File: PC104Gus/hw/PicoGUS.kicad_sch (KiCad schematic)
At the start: 37 parts, among them J1 Conn_02x32_Odd_Even, J11 AudioJack3, J12 AudioJack3, J3 Conn_01x02_Pin, J4 IRQDMA_JP, J5 Conn_01x04_Pin, J6 UART_TX, U1 SN74CB3T3257, U10 74LVC1G00, U2 SN74CB3T3257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

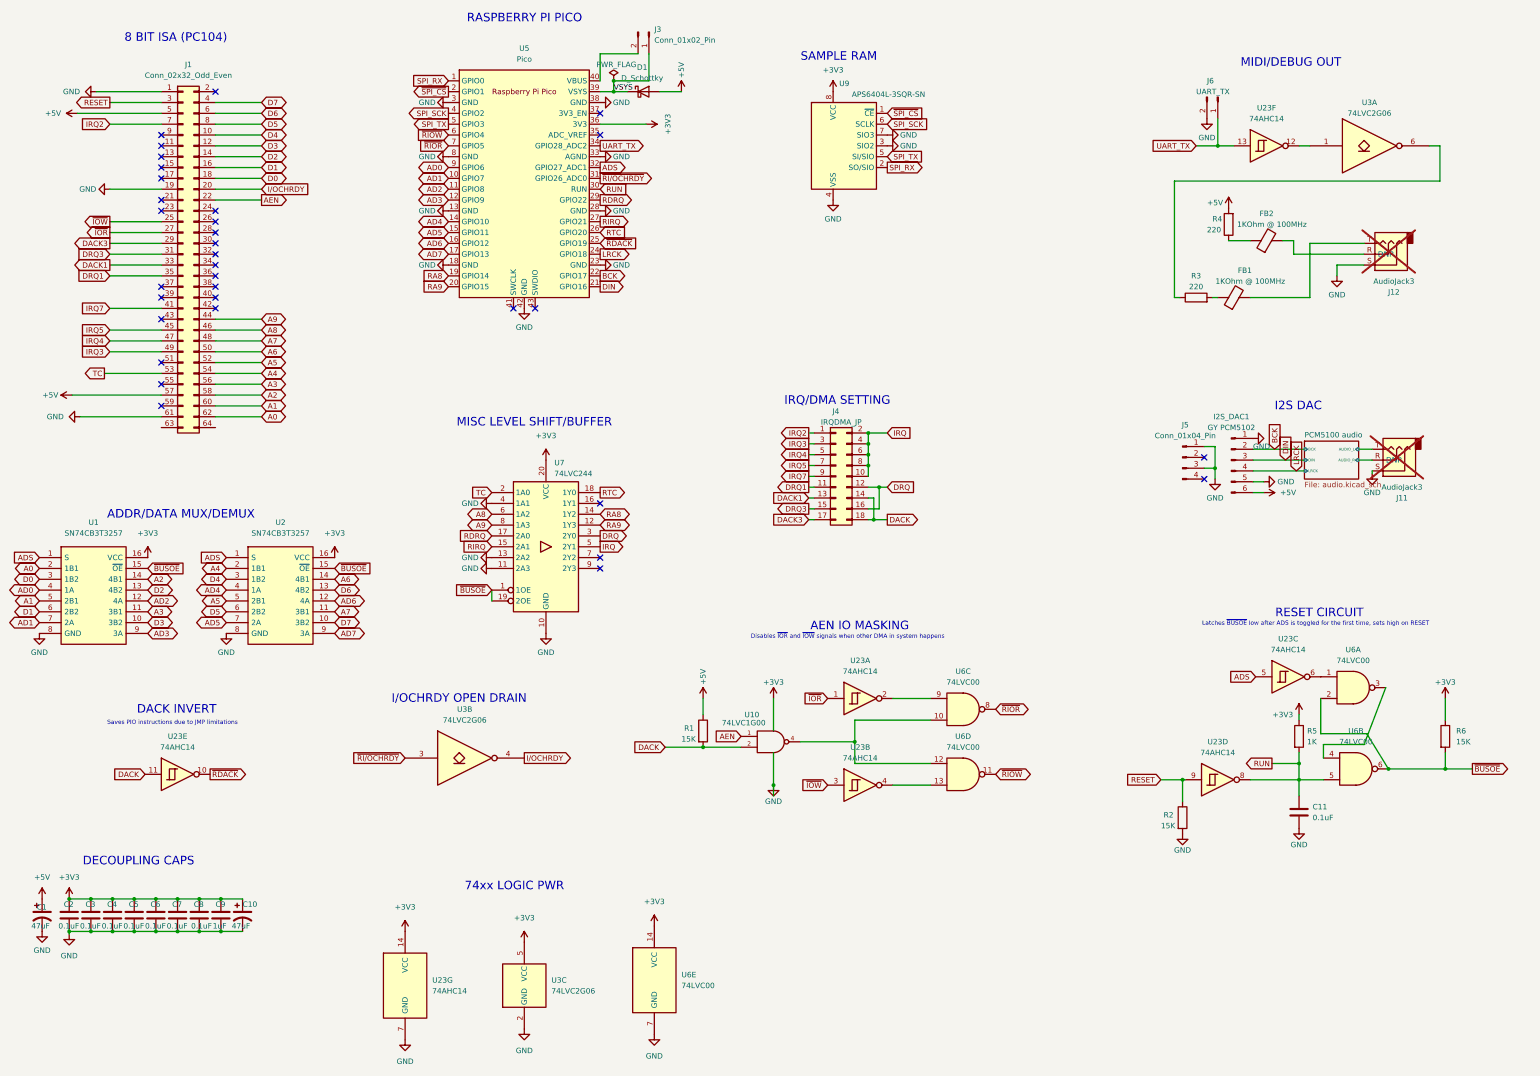
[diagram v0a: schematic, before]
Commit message: PC104GUS production files
Production files generated. This build worked!
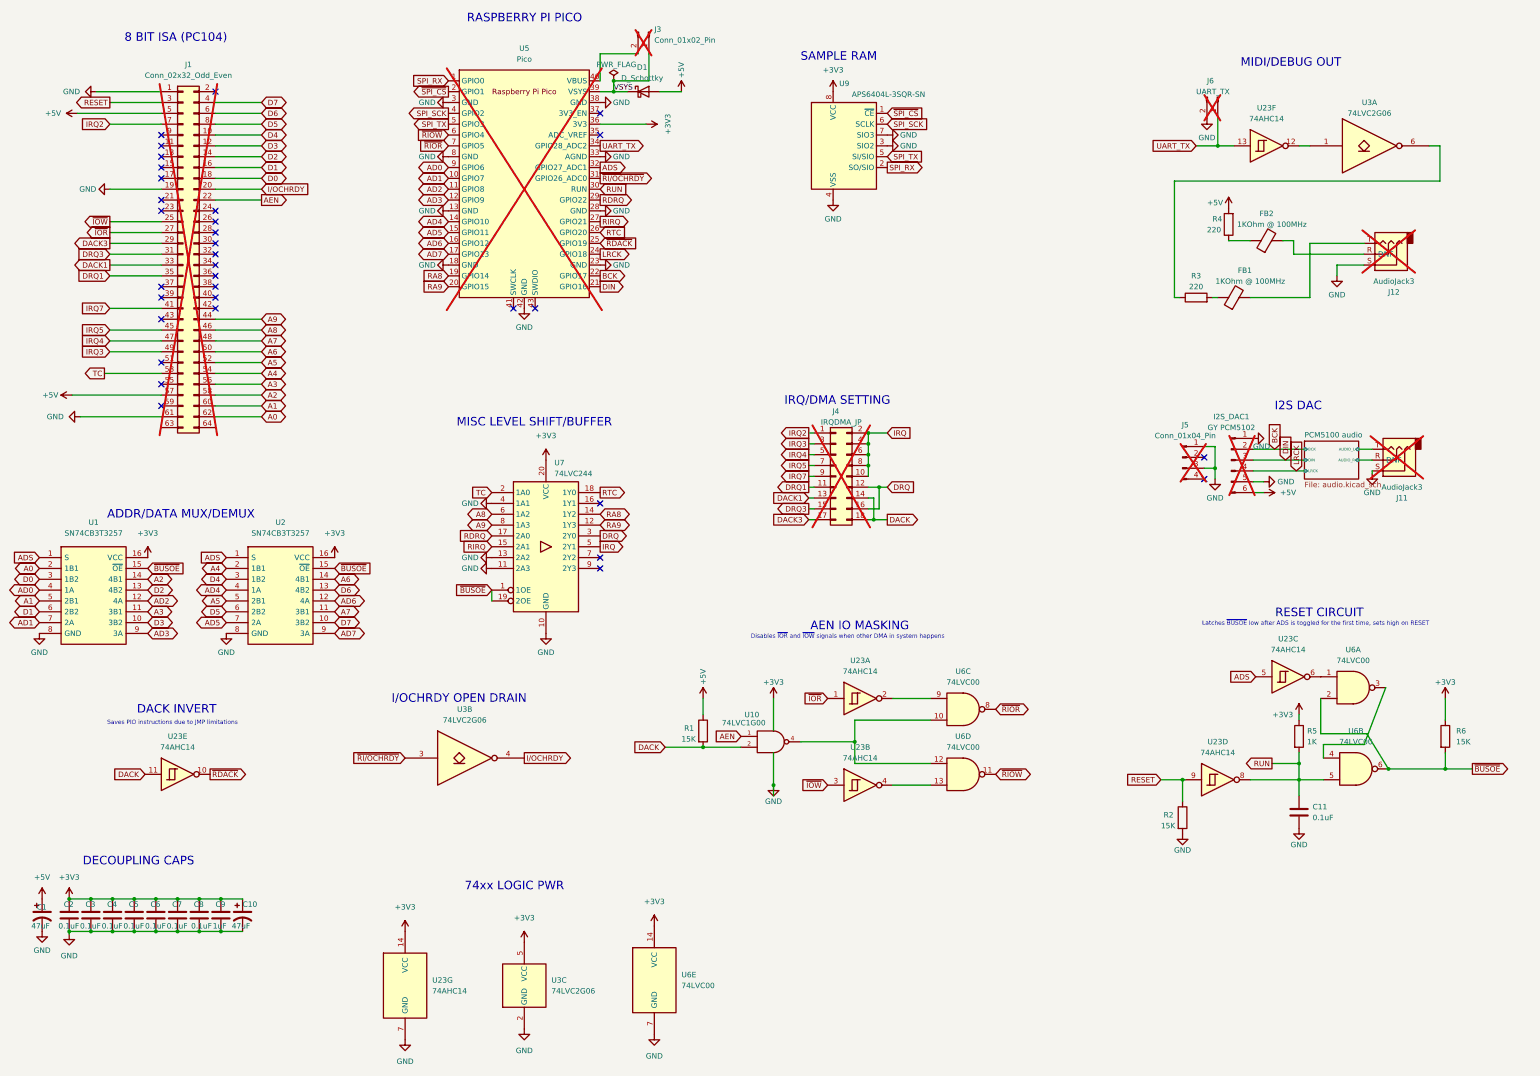
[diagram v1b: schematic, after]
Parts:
- I2S_DAC1, J1, J3, J5, J6: LCSC (none) -> DNF; now not fitted
- J11, J12: LCSC DNP -> DNF
- J4: LCSC C492426 -> DNF; now not fitted
- U23: LCSC (none) -> C5510
- U3: LCSC (none) -> C402162
- U5: LCSC C2905423 -> DNF; now not fitted
- U6: LCSC (none) -> C526338
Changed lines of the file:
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@@
 			)
 		)
+		(property "LCSC" "C402162"
+			(at 163.83 262.89 0)
+			(effects
+				(font
+					(size 1.27 1.27)
+				)
+				(hide yes)
+			)
+		)
 		(pin "3"
 		)
@@
 			)
 		)
+		(property "LCSC" "C5510"
+			(at 337.82 66.04 0)
+			(effects
+				(font
+					(size 1.27 1.27)
+				)
+				(hide yes)
+			)
+		)
 		(pin "6"
 		)
@@
 			)
 		)
+		(property "LCSC" "C5510"
+			(at 326.39 214.63 0)
+			(effects
+				(font
+					(size 1.27 1.27)
+				)
+				(hide yes)
+			)
+		)
 		(pin "6"
 		)
@@
 		(in_bom yes)
 		(on_board yes)
-		(dnp no)
+		(dnp yes)
 		(property "Reference" "I2S_DAC1"
 			(at 329.565 129.54 0)
@@
 			)
 		)
+		(property "LCSC" "DNF"
+			(at 329.565 139.7 0)
+			(effects
+				(font
+					(size 1.27 1.27)
+				)
+				(hide yes)
+			)
+		)
 		(pin "1"
 		)
@@
 			)
 		)
+		(property "LCSC" "C526338"
+			(at 194.31 261.62 0)
+			(effects
+				(font
+					(size 1.27 1.27)
+				)
+				(hide yes)
+			)
+		)
 		(pin "13"
 		)
@@
 		(in_bom yes)
 		(on_board yes)
-		(dnp no)
+		(dnp yes)
 		(fields_autoplaced yes)
 		(property "Reference" "J3"
@@
 			)
 		)
+		(property "LCSC" "DNF"
+			(at 193.04 39.37 90)
+			(effects
+				(font
+					(size 1.27 1.27)
+				)
+				(hide yes)
+			)
+		)
 		(pin "1"
 		)
@@
 			)
 		)
+		(property "LCSC" "C402162"
+			(at 363.22 66.04 0)
+			(effects
+				(font
+					(size 1.27 1.27)
+				)
+				(hide yes)
+			)
+		)
 		(pin "3"
 		)
@@
 		(in_bom yes)
 		(on_board yes)
-		(dnp no)
+		(dnp yes)
 		(fields_autoplaced yes)
 		(property "Reference" "U5"
@@
 			)
 		)
-		(property "LCSC" "C2905423"
+		(property "LCSC" "DNF"
 			(at 163.83 43.18 0)
 			(effects
@@
 			)
 		)
+		(property "LCSC" "C526338"
+			(at 358.775 212.09 0)
+			(effects
+				(font
+					(size 1.27 1.27)
+				)
+				(hide yes)
+			)
+		)
 		(pin "13"
 		)
@@
 			)
 		)
+		(property "LCSC" "C526338"
+			(at 266.7 198.12 0)
+			(effects
+				(font
+					(size 1.27 1.27)
+				)
+				(hide yes)
+			)
+		)
 		(pin "13"
 		)
@@
 			)
 		)
+		(property "LCSC" "C402162"
+			(at 151.13 209.55 0)
+			(effects
+				(font
+					(size 1.27 1.27)
+				)
+				(hide yes)
+			)
+		)
 		(pin "3"
 		)
@@
 			)
 		)
+		(property "LCSC" "C5510"
+			(at 242.57 215.9 0)
+			(effects
+				(font
+					(size 1.27 1.27)
+				)
+				(hide yes)
+			)
+		)
 		(pin "6"
 		)
@@
 			)
 		)
+		(property "LCSC" "C526338"
+			(at 358.14 193.04 0)
+			(effects
+				(font
+					(size 1.27 1.27)
+				)
+				(hide yes)
+			)
+		)
 		(pin "13"
 		)
@@
 		(in_bom yes)
 		(on_board yes)
-		(dnp no)
+		(dnp yes)
 		(property "Reference" "J4"
 			(at 236.855 128.27 0)
@@
 			)
 		)
-		(property "LCSC" "C492426"
+		(property "LCSC" "DNF"
 			(at 236.855 128.27 0)
 			(effects
@@
 			)
 		)
+		(property "LCSC" "C5510"
+			(at 82.55 213.36 0)
+			(effects
+				(font
+					(size 1.27 1.27)
+				)
+				(hide yes)
+			)
+		)
 		(pin "6"
 		)
@@
 		(in_bom yes)
 		(on_board yes)
-		(dnp no)
+		(dnp yes)
 		(fields_autoplaced yes)
 		(property "Reference" "J5"
@@
 			)
 		)
+		(property "LCSC" "DNF"
+			(at 318.135 139.065 0)
+			(effects
+				(font
+					(size 1.27 1.27)
+				)
+				(hide yes)
+			)
+		)
 		(pin "1"
 		)
@@
 			)
 		)
+		(property "LCSC" "C5510"
+			(at 242.57 195.58 0)
+			(effects
+				(font
+					(size 1.27 1.27)
+				)
+				(hide yes)
+			)
+		)
 		(pin "6"
 		)
@@
 		(in_bom yes)
 		(on_board yes)
-		(dnp no)
+		(dnp yes)
 		(property "Reference" "J6"
 			(at 323.85 50.8 90)
@@
 			)
 		)
+		(property "LCSC" "DNF"
+			(at 326.39 54.61 90)
+			(effects
+				(font
+					(size 1.27 1.27)
+				)
+				(hide yes)
+			)
+		)
 		(pin "1"
 		)
@@
 			)
 		)
-		(property "LCSC" "DNP"
+		(property "LCSC" "DNF"
 			(at 367.665 139.7 0)
 			(effects
@@
 			)
 		)
+		(property "LCSC" "C526338"
+			(at 266.7 213.36 0)
+			(effects
+				(font
+					(size 1.27 1.27)
+				)
+				(hide yes)
+			)
+		)
 		(pin "13"
 		)
@@
 			)
 		)
-		(property "LCSC" "DNP"
+		(property "LCSC" "DNF"
 			(at 365.76 91.44 0)
 			(effects
@@
 		(in_bom yes)
 		(on_board yes)
-		(dnp no)
+		(dnp yes)
 		(fields_autoplaced yes)
 		(property "Reference" "J1"
@@
 			)
 		)
+		(property "LCSC" "DNF"
+			(at 83.82 91.44 0)
+			(effects
+				(font
+					(size 1.27 1.27)
+				)
+				(hide yes)
+			)
+		)
 		(pin "31"
 		)
@@
 			)
 		)
+		(property "LCSC" "C5510"
+			(at 135.89 262.89 0)
+			(effects
+				(font
+					(size 1.27 1.27)
+				)
+				(hide yes)
+			)
+		)
 		(pin "6"
 		)
@@
 			(at 342.9 190.5 0)
 			(effects
+				(font
+					(size 1.27 1.27)
+				)
+				(hide yes)
+			)
+		)
+		(property "LCSC" "C5510"
+			(at 342.9 190.5 0)
+			(effects
